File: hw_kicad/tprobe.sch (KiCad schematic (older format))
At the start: 28 parts, among them IC1 ATTINY85-P, P1 INPUT, P2 PRB_GND, P3 PRB_VCC, P4 AVR_ISP, P5 FTDI_CN, P6 MLIPO, SW1 SW_PUSH_SMALL_H

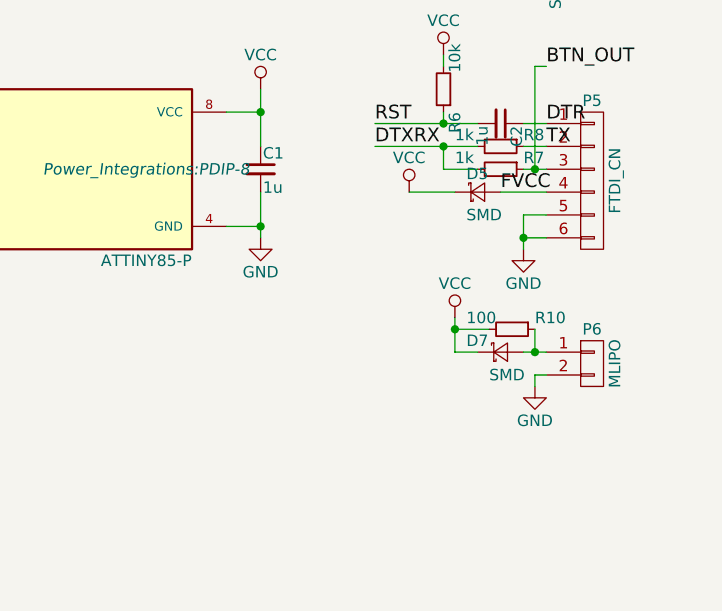
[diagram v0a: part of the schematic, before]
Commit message: It deserves a real li-ion charger :)
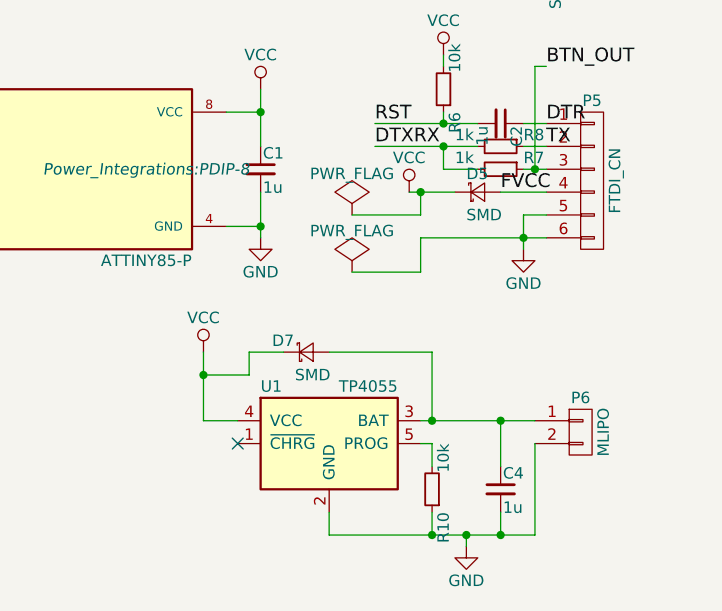
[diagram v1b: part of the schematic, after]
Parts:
- added C4: 1u, Capacitors_SMD:C_0603_HandSoldering, symbol C_Small
- added U1: TP4055, TO_SOT_Packages_SMD:SOT-23-5, symbol TP4055
- R10: value 100 -> 10k
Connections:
- net GND: now also R10.1, C4.2, U1.2 (GND)
- net VCC: now also U1.4 (VCC); no longer R10.2
- net at D7.2 (A), P6.1 (P1): now also C4.1, U1.3 (BAT); no longer R10.1
- new net: R10.2, U1.5 (PROG)
- no-connect marks 0 -> 1
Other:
- moved on the sheet: D7, P6, R10
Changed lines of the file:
@@
 LIBS:contrib
 LIBS:valves
+LIBS:tp4055
+LIBS:tprobe-cache
 EELAYER 25 0
 EELAYER END
@@
 $EndComp
 Wire Wire Line
-	8550 4150 8450 4150
+	8000 4150 8550 4150
 Wire Wire Line
 	8450 4050 8450 4200
@@
 L CONN_01X02 P6
 U 1 1 585FD3AE
-P 8750 4700
-F 0 "P6" H 8750 4850 50  0000 C CNN
-F 1 "MLIPO" V 8850 4700 50  0000 C CNN
-F 2 "Pin_Headers:Pin_Header_Straight_1x02" H 8750 4700 50  0001 C CNN
-F 3 "" H 8750 4700 50  0000 C CNN
-	1    8750 4700
+P 8700 5000
+F 0 "P6" H 8700 5150 50  0000 C CNN
+F 1 "MLIPO" V 8800 5000 50  0000 C CNN
+F 2 "Pin_Headers:Pin_Header_Straight_1x02" H 8700 5000 50  0001 C CNN
+F 3 "" H 8700 5000 50  0000 C CNN
+	1    8700 5000
 	1    0    0    -1
 $EndComp
@@
 L GND #PWR013
 U 1 1 585FD4CE
-P 8500 4800
-F 0 "#PWR013" H 8500 4550 50  0001 C CNN
-F 1 "GND" H 8500 4650 50  0000 C CNN
-F 2 "" H 8500 4800 50  0000 C CNN
-F 3 "" H 8500 4800 50  0000 C CNN
-	1    8500 4800
-	1    0    0    -1
-$EndComp
-Wire Wire Line
-	8500 4800 8500 4750
-Wire Wire Line
-	8500 4750 8550 4750
+P 8200 5500
+F 0 "#PWR013" H 8200 5250 50  0001 C CNN
+F 1 "GND" H 8200 5350 50  0000 C CNN
+F 2 "" H 8200 5500 50  0000 C CNN
+F 3 "" H 8200 5500 50  0000 C CNN
+	1    8200 5500
+	1    0    0    -1
+$EndComp
 $Comp
 L D_Schottky_Small D7
 U 1 1 585FD612
-P 8350 4650
-F 0 "D7" H 8200 4700 50  0000 L CNN
-F 1 "SMD" H 8300 4550 50  0000 L CNN
-F 2 "Diodes_SMD:SOD-323_HandSoldering" V 8350 4650 50  0001 C CNN
-F 3 "" V 8350 4650 50  0000 C CNN
-	1    8350 4650
-	1    0    0    -1
-$EndComp
-Wire Wire Line
-	8450 4650 8550 4650
+P 7500 4650
+F 0 "D7" H 7350 4700 50  0000 L CNN
+F 1 "SMD" H 7450 4550 50  0000 L CNN
+F 2 "Diodes_SMD:SOD-323_HandSoldering" V 7500 4650 50  0001 C CNN
+F 3 "" V 7500 4650 50  0000 C CNN
+	1    7500 4650
+	1    0    0    -1
+$EndComp
 $Comp
 L VCC #PWR014
 U 1 1 585FD775
-P 8150 4500
-F 0 "#PWR014" H 8150 4350 50  0001 C CNN
-F 1 "VCC" H 8150 4650 50  0000 C CNN
-F 2 "" H 8150 4500 50  0000 C CNN
-F 3 "" H 8150 4500 50  0000 C CNN
-	1    8150 4500
-	1    0    0    -1
-$EndComp
-Wire Wire Line
-	8150 4650 8250 4650
-Wire Wire Line
-	8150 4500 8150 4650
+P 7050 4650
+F 0 "#PWR014" H 7050 4500 50  0001 C CNN
+F 1 "VCC" H 7050 4800 50  0000 C CNN
+F 2 "" H 7050 4650 50  0000 C CNN
+F 3 "" H 7050 4650 50  0000 C CNN
+	1    7050 4650
+	1    0    0    -1
+$EndComp
 $Comp
 L R_Small R10
 U 1 1 585FD9D3
-P 8400 4550
-F 0 "R10" V 8350 4650 50  0000 L CNN
-F 1 "100" V 8350 4350 50  0000 L CNN
-F 2 "Resistors_SMD:R_0603_HandSoldering" H 8400 4550 50  0001 C CNN
-F 3 "" H 8400 4550 50  0000 C CNN
-	1    8400 4550
-	0    1    1    0
-$EndComp
-Wire Wire Line
-	8500 4550 8500 4650
-Connection ~ 8500 4650
-Wire Wire Line
-	8300 4550 8150 4550
-Connection ~ 8150 4550
+P 8050 5250
+F 0 "R10" V 8000 5350 50  0000 L CNN
+F 1 "10k" V 8000 5050 50  0000 L CNN
+F 2 "Resistors_SMD:R_0603_HandSoldering" H 8050 5250 50  0001 C CNN
+F 3 "" H 8050 5250 50  0000 C CNN
+	1    8050 5250
+	-1   0    0    1
+$EndComp
+$Comp
+L TP4055 U1
+U 1 1 58D7CC94
+P 7600 5050
+F 0 "U1" H 7300 5300 50  0000 L CNN
+F 1 "TP4055" H 7900 5300 50  0000 R CNN
+F 2 "TO_SOT_Packages_SMD:SOT-23-5" H 7600 4650 50  0001 C CNN
+F 3 "" H 7600 5050 50  0000 C CNN
+	1    7600 5050
+	1    0    0    -1
+$EndComp
+$Comp
+L C_Small C4
+U 1 1 58D7D41D
+P 8350 5250
+F 0 "C4" H 8360 5320 50  0000 L CNN
+F 1 "1u" H 8360 5170 50  0000 L CNN
+F 2 "Capacitors_SMD:C_0603_HandSoldering" H 8350 5250 50  0001 C CNN
+F 3 "" H 8350 5250 50  0000 C CNN
+	1    8350 5250
+	1    0    0    -1
+$EndComp
+Wire Wire Line
+	8050 5350 8050 5450
+Wire Wire Line
+	7600 5450 8500 5450
+Wire Wire Line
+	8350 5450 8350 5350
+Wire Wire Line
+	8200 5450 8200 5500
+Connection ~ 8200 5450
+Wire Wire Line
+	7600 5450 7600 5350
+Connection ~ 8050 5450
+Wire Wire Line
+	8000 5050 8050 5050
+Wire Wire Line
+	8050 5050 8050 5150
+Wire Wire Line
+	8500 5450 8500 5050
+Connection ~ 8350 5450
+Wire Wire Line
+	8500 4950 8000 4950
+Wire Wire Line
+	8350 5150 8350 4950
+Connection ~ 8350 4950
+Wire Wire Line
+	7050 4950 7200 4950
+Wire Wire Line
+	7050 4650 7050 4950
+Wire Wire Line
+	7400 4650 7250 4650
+Wire Wire Line
+	7250 4650 7250 4750
+Wire Wire Line
+	7250 4750 7050 4750
+Connection ~ 7050 4750
+Wire Wire Line
+	7600 4650 8050 4650
+Wire Wire Line
+	8050 4650 8050 4950
+Connection ~ 8050 4950
+$Comp
+L PWR_FLAG #FLG015
+U 1 1 58D821B4
+P 7700 4050
+F 0 "#FLG015" H 7700 4145 50  0001 C CNN
+F 1 "PWR_FLAG" H 7700 4230 50  0000 C CNN
+F 2 "" H 7700 4050 50  0000 C CNN
+F 3 "" H 7700 4050 50  0000 C CNN
+	1    7700 4050
+	1    0    0    -1
+$EndComp
+Wire Wire Line
+	7700 4050 8000 4050
+Wire Wire Line
+	8000 4050 8000 3950
+Connection ~ 8000 3950
+$Comp
+L PWR_FLAG #FLG016
+U 1 1 58D828E7
+P 7700 4300
+F 0 "#FLG016" H 7700 4395 50  0001 C CNN
+F 1 "PWR_FLAG" H 7700 4480 50  0000 C CNN
+F 2 "" H 7700 4300 50  0000 C CNN
+F 3 "" H 7700 4300 50  0000 C CNN
+	1    7700 4300
+	1    0    0    -1
+$EndComp
+Wire Wire Line
+	7700 4300 8000 4300
+Wire Wire Line
+	8000 4300 8000 4150
+NoConn ~ 7200 5050
 $EndSCHEMATC
